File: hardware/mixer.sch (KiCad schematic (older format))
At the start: 31 parts, among them U26 5400BL15B050E, U27 5400BL15B050E, U28 5400BL15B050E, U29 ADL5802

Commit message: Improved documentation and added schematics to default libraries.
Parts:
- removed F1, F2: Via, fmcw:RF_via, symbol fmcw-rescue:Via-fmcw3-rescue
- removed U26, U27, U28: 5400BL15B050E, fmcw:5400BL15B050E, symbol fmcw-rescue:5400BL15B050E-fmcw3-rescue
- added U26, U27, U28: 5400BL15B050E, RF_Converter:Balun_Johanson_5400BL15B050E, symbol Transformer:5400BL15B050
- U29: footprint Package_DFN_QFN:QFN-24-1EP_4x4mm_P0.5mm_EP2.6x2.6mm -> Package_CSP:LFCSP-WQ-24-7EP_4x4mm_P0.5mm_EP2.6416x2.6416mm; symbol fmcw-rescue:ADL5802-fmcw3-rescue -> RF_Mixer:ADL5802
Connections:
- wire segments 121 -> 94
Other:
- moved on the sheet: C107, C109, C110, C111, C112, C113, C114, C122, C123, R49, R50, R53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

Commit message: Improved tx sheet and corresponding documentation.
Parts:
- U29: symbol RF_Mixer:ADL5802 -> fmcw-rescue:ADL5802-RF_Mixer
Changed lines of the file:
@@
 IF1-
 $Comp
-L RF_Mixer:ADL5802 U?
+L fmcw-rescue:ADL5802-RF_Mixer U?
 U 1 1 5942E974
 P 5600 4350

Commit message: Improved documentation and parts of the schematic.
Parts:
- C107: value DNP -> 100n; footprint Capacitor_SMD:C_0805_2012Metric -> Capacitor_SMD:C_0402_1005Metric; MFN (none) -> CL05B104KO5NNNC
- U29: footprint Package_CSP:LFCSP-WQ-24-7EP_4x4mm_P0.5mm_EP2.6416x2.6416mm -> Package_CSP:LFCSP-24-1EP_4x4mm_P0.5mm_EP2.5x2.5mm; symbol fmcw-rescue:ADL5802-RF_Mixer -> RF_Mixer:ADL5802
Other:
- moved on the sheet: C119, C120, C121, R49, R50, R51, R52

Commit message: Finished design, began routing.
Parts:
- added C250: 100n, Capacitor_SMD:C_0402_1005Metric, symbol Device:C
- C218: renamed from C111; MFN 500R07S3R0BV4T -> 500R07S3R0BV4T
- C219: renamed from C112; MFN 500R07S3R0BV4T -> 500R07S3R0BV4T
- C220: renamed from C109; MFN 500R07S3R0BV4T -> 500R07S3R0BV4T
- C221: renamed from C110; MFN 500R07S3R0BV4T -> 500R07S3R0BV4T
- C222: renamed from C113; MFN 500R07S3R0BV4T -> 500R07S3R0BV4T
- C223: renamed from C114; MFN 500R07S3R0BV4T -> 500R07S3R0BV4T
- U35: renamed from U26; MFN (none) -> 5400BL15B050E
- U36: renamed from U27; MFN (none) -> 5400BL15B050E
- U37: renamed from U28; MFN (none) -> 5400BL15B050E
- renumbered C107 to C215, C108 to C216, C115 to C217, C116 to C224, C117 to C225, C118 to C226, C119 to C227, C162 to C228, C122 to C229, C123 to C230, C120 to C231, C121 to C232, FB13 to FB16, R49 to R67, R50 to R68, R53 to R69, R54 to R70, R51 to R71, R52 to R72, U29 to U38
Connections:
- net 5VF: now also C250.2
- net GND: now also C250.1
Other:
- moved on the sheet: C215, FB16

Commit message: Completed clock placement and routing.
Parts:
- removed C250: 100n, Capacitor_SMD:C_0402_1005Metric, symbol Device:C
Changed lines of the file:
@@
 	1950 2700 1950 2800
 Wire Wire Line
-	2400 2200 2550 2200
-$Comp
-L Device:C C250
-U 1 1 5C60A0E1
-P 2550 2550
-F 0 "C250" H 2664 2504 50  0000 L CNN
-F 1 "100n" H 2664 2595 50  0000 L CNN
-F 2 "Capacitor_SMD:C_0402_1005Metric" H 2588 2400 30  0001 C CNN
-F 3 "" H 2550 2550 60  0000 C CNN
-F 4 "CL05B104KO5NNNC" H -900 -50 50  0001 C CNN "MFN"
-	1    2550 2550
-	-1   0    0    1
-$EndComp
-Wire Wire Line
-	2550 2400 2550 2200
-Connection ~ 2550 2200
-Wire Wire Line
-	2550 2200 4150 2200
-$Comp
-L power:GND #PWR0262
-U 1 1 5C60D1E6
-P 2550 2800
-F 0 "#PWR0262" H 2550 2550 50  0001 C CNN
-F 1 "GND" H 2550 2650 50  0000 C CNN
-F 2 "" H 2550 2800 60  0000 C CNN
-F 3 "" H 2550 2800 60  0000 C CNN
-	1    2550 2800
-	1    0    0    -1
-$EndComp
-Wire Wire Line
-	2550 2800 2550 2700
+	2400 2200 4150 2200
 $EndSCHEMATC

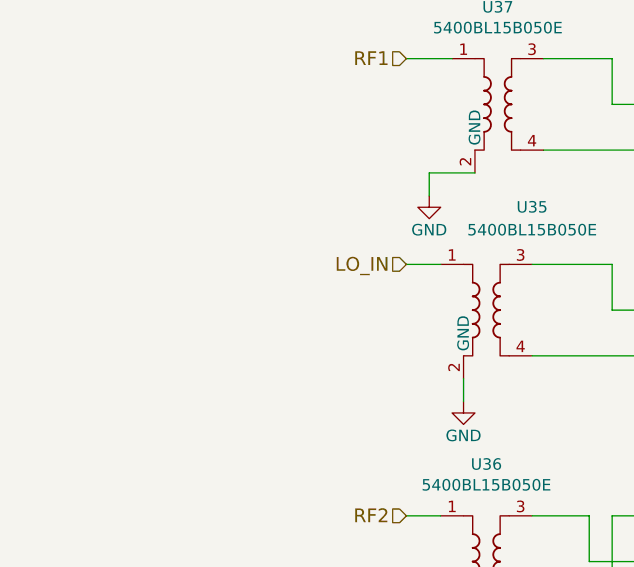
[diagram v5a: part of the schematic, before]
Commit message: Completed FPGA bypassing.
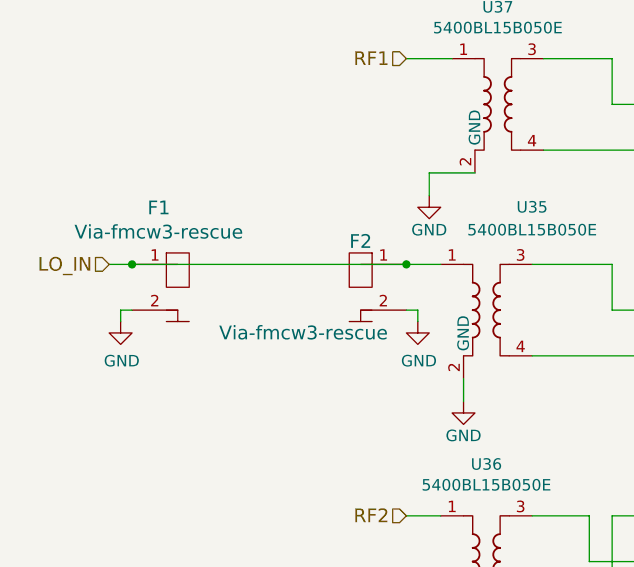
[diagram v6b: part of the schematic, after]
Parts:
- added F1, F2: Via-fmcw3-rescue, fmcw:RF_via, symbol fmcw-rescue:Via-fmcw3-rescue
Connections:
- net GND: now also F1.2, F2.2
- net LO_IN: now also F1.1, F2.1
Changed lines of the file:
@@
 Text HLabel 5000 4850 0    60   Input ~ 0
 MIX_ENBL
-Text HLabel 2600 4200 0    60   Input ~ 0
+Text HLabel 1300 4200 0    60   Input ~ 0
 LO_IN
 Text HLabel 8600 3750 2    60   Output ~ 0
@@
 	3400 5500 3700 5500
 Wire Wire Line
-	2750 4200 2600 4200
-Wire Wire Line
 	2700 3800 2900 3800
 Wire Wire Line
@@
 Wire Wire Line
 	2400 2200 4150 2200
+Wire Wire Line
+	1400 4400 1350 4400
+Wire Wire Line
+	1350 4400 1350 4450
+$Comp
+L power:GND #PWR013
+U 1 1 5C68B882
+P 1350 4450
+F 0 "#PWR013" H 1350 4200 50  0001 C CNN
+F 1 "GND" H 1355 4277 50  0000 C CNN
+F 2 "" H 1350 4450 50  0001 C CNN
+F 3 "" H 1350 4450 50  0001 C CNN
+	1    1350 4450
+	1    0    0    -1
+$EndComp
+Wire Wire Line
+	2600 4400 2650 4400
+Wire Wire Line
+	2650 4400 2650 4450
+$Comp
+L power:GND #PWR014
+U 1 1 5C68EEE7
+P 2650 4450
+F 0 "#PWR014" H 2650 4200 50  0001 C CNN
+F 1 "GND" H 2655 4277 50  0000 C CNN
+F 2 "" H 2650 4450 50  0001 C CNN
+F 3 "" H 2650 4450 50  0001 C CNN
+	1    2650 4450
+	1    0    0    -1
+$EndComp
+Wire Wire Line
+	1300 4200 1400 4200
+$Comp
+L fmcw-rescue:Via-fmcw3-rescue F1
+U 1 1 5C6849A7
+P 1600 4200
+F 0 "F1" H 1517 4447 60  0000 C CNN
+F 1 "Via-fmcw3-rescue" H 1517 4341 60  0000 C CNN
+F 2 "fmcw:RF_via" H 1600 4200 60  0001 C CNN
+F 3 "" H 1600 4200 60  0001 C CNN
+	1    1600 4200
+	1    0    0    -1
+$EndComp
+$Comp
+L fmcw-rescue:Via-fmcw3-rescue F2
+U 1 1 5C683DA9
+P 2400 4200
+F 0 "F2" H 2400 4300 60  0000 C CNN
+F 1 "Via-fmcw3-rescue" H 2650 3900 60  0000 C CNN
+F 2 "fmcw:RF_via" H 2400 4200 60  0001 C CNN
+F 3 "" H 2400 4200 60  0001 C CNN
+	1    2400 4200
+	-1   0    0    -1
+$EndComp
+Wire Wire Line
+	1400 4200 2600 4200
+Connection ~ 1400 4200
+Connection ~ 2600 4200
+Wire Wire Line
+	2600 4200 2750 4200
 $EndSCHEMATC

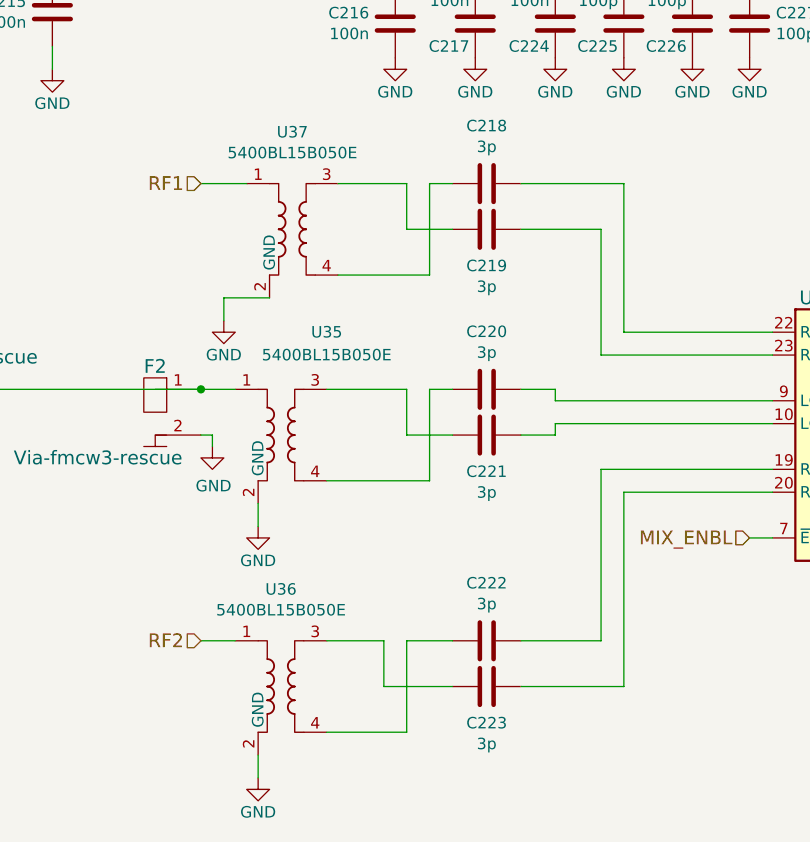
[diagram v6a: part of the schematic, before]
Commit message: Better MFNs for RF DC blocking caps.
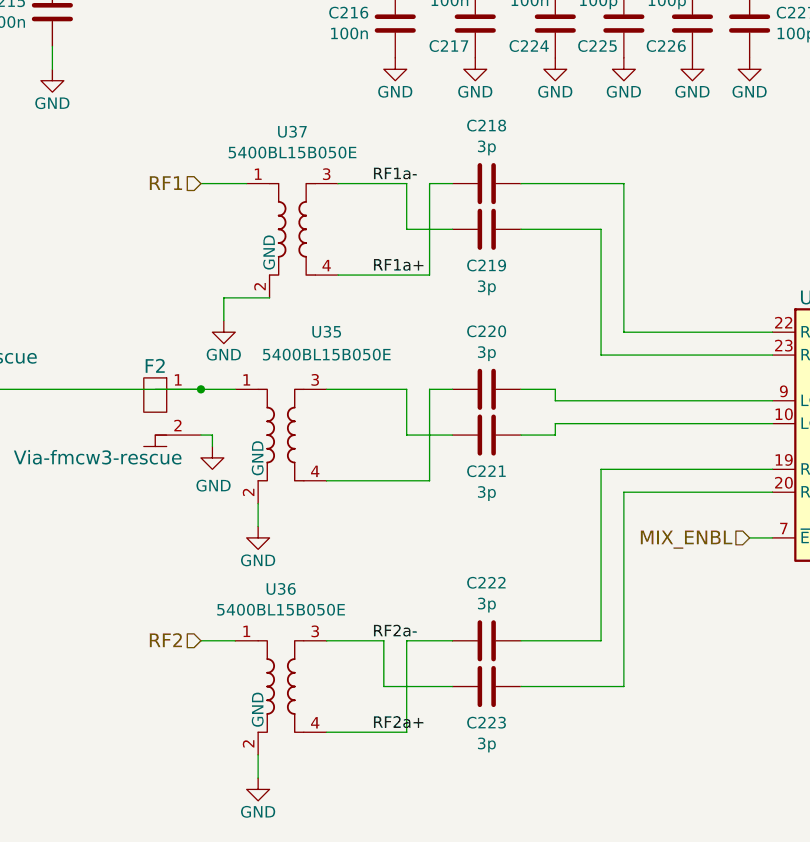
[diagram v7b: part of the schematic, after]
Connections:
- net RF1a+: now reaches C218.2, U37.4
- net RF1a-: now reaches C219.2, U37.3
- net RF2a+: now reaches C222.2, U36.4
- net RF2a-: now reaches C223.2, U36.3
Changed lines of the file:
@@
 Wire Wire Line
 	2600 4200 2750 4200
+Text Label 3350 3300 0    50   ~ 0
+RF1a-
+Text Label 3350 3700 0    50   ~ 0
+RF1a+
+Text Label 3350 5300 0    50   ~ 0
+RF2a-
+Text Label 3350 5700 0    50   ~ 0
+RF2a+
 $EndSCHEMATC

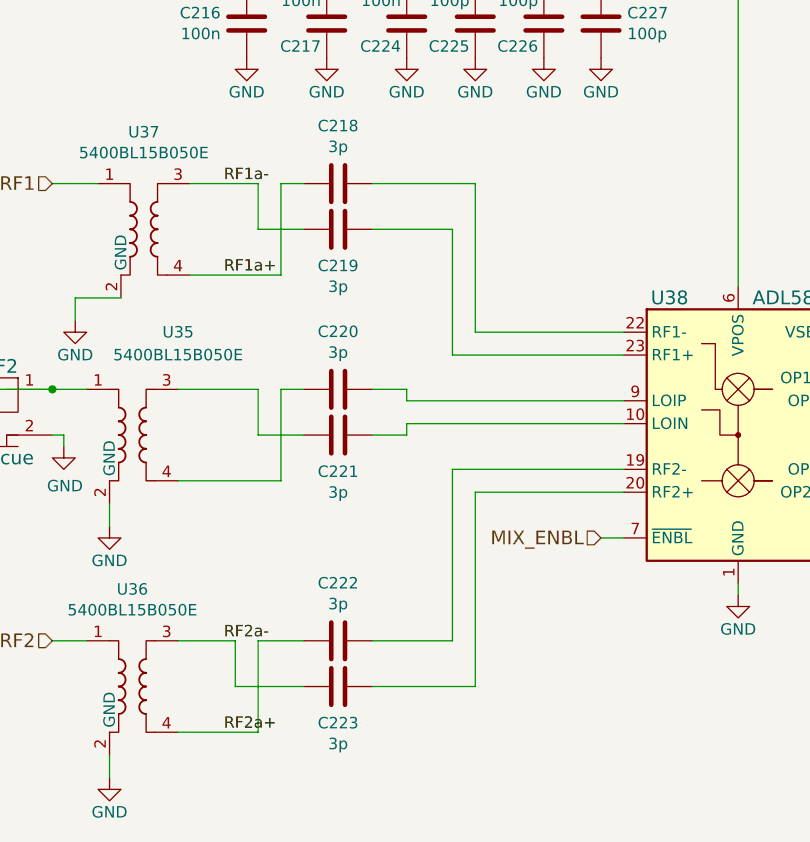
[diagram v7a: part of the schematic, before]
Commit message: Completed transmitter placement/routing.
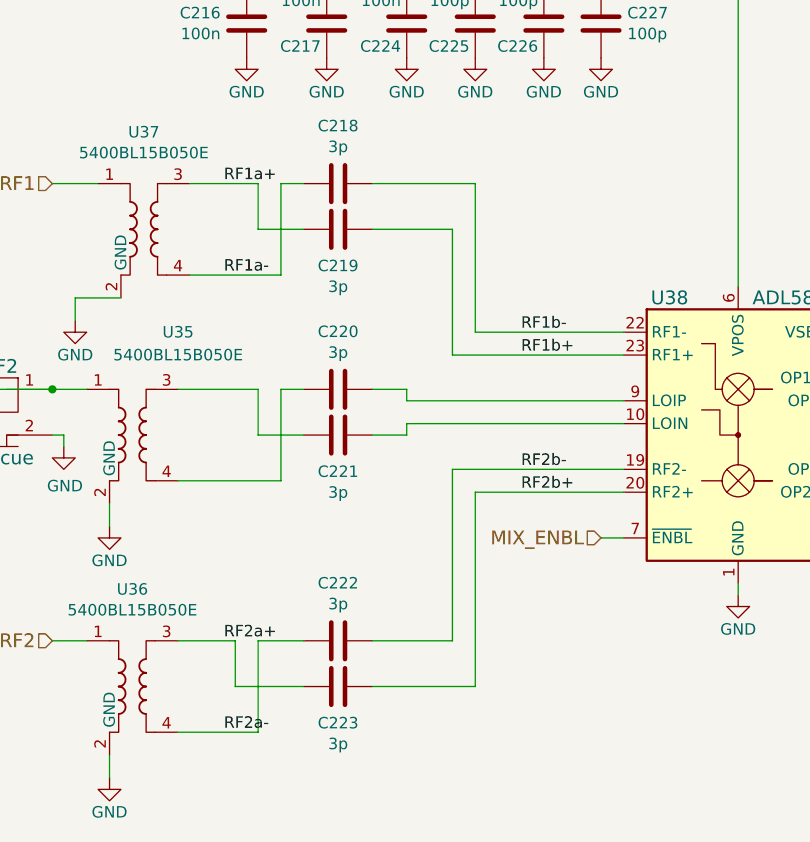
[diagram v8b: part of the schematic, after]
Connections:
- net RF1a+: now also C219.2, U37.3; no longer C218.2, U37.4
- net RF1a-: now also C218.2, U37.4; no longer C219.2, U37.3
- net RF2a+: now also C223.2, U36.3; no longer C222.2, U36.4
- net RF2a-: now also C222.2, U36.4; no longer C223.2, U36.3
- net RF2b-: now reaches C222.1, U38.19 (RF2-)
- net RF2b+: now reaches C223.1, U38.20 (RF2+)
- net RF1b-: now reaches C218.1, U38.22 (RF1-)
- net RF1b+: now reaches C219.1, U38.23 (RF1+)
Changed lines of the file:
@@
 Wire Wire Line
 	2600 4200 2750 4200
+Text Label 3350 3700 0    50   ~ 0
+RF1a-
 Text Label 3350 3300 0    50   ~ 0
-RF1a-
-Text Label 3350 3700 0    50   ~ 0
 RF1a+
+Text Label 3350 5700 0    50   ~ 0
+RF2a-
 Text Label 3350 5300 0    50   ~ 0
-RF2a-
-Text Label 3350 5700 0    50   ~ 0
 RF2a+
+Text Label 4650 4050 0    50   ~ 0
+RF1b+
+Text Label 4650 3950 0    50   ~ 0
+RF1b-
+Text Label 4650 4650 0    50   ~ 0
+RF2b+
+Text Label 4650 4550 0    50   ~ 0
+RF2b-
 $EndSCHEMATC
